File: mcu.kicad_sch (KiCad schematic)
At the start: 25 parts, among them J1 Conn_01x05, J4 USB_B_Micro, U1 STM32G473CCUx, Y1 8 MHz

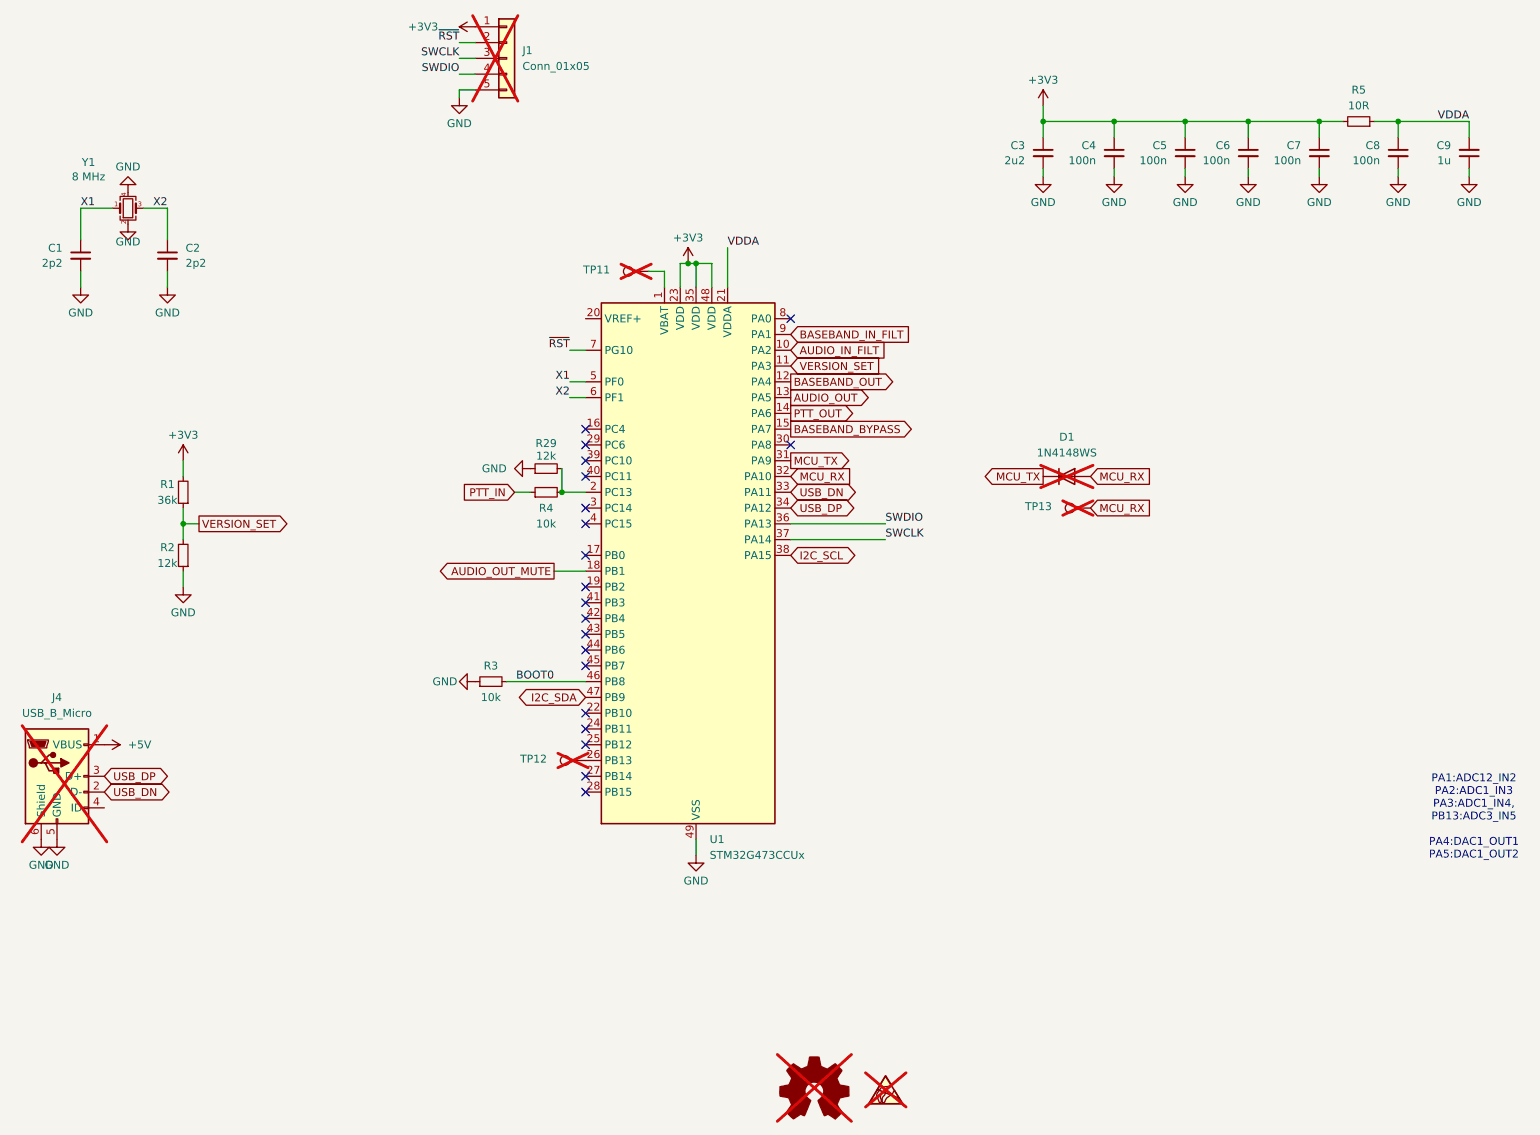
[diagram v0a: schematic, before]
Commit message: cosmetic changes to the schematic layout
- R25 - DNP
- PDF render update
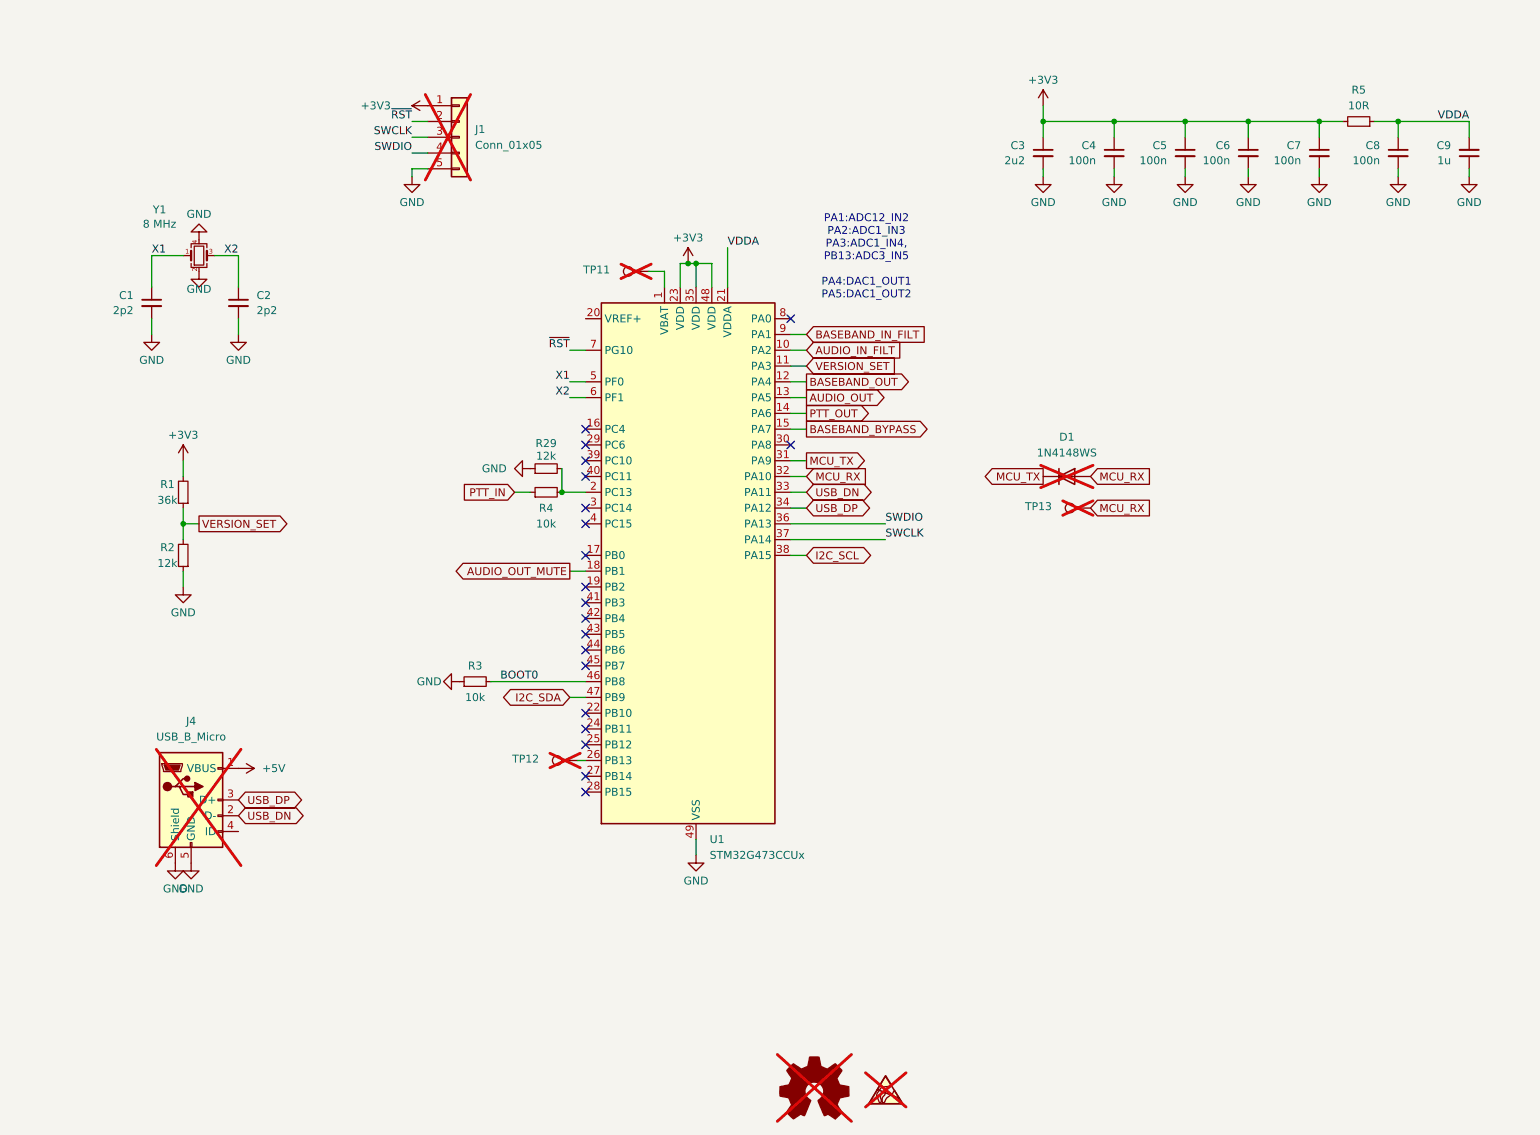
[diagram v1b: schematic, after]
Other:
- company: Wojciech Kaczmarski SP5WWP et al. -> Wojciech SP5WWP, Mano ON6RF, Mutlu TA1MD et al.
- title: Micro17 - OpenRTX on a Module for Icom Radios -> Micro17 - OpenRTX on a Module for ICOM radios
- moved on the sheet: C1, C2, J1, J4, R3, TP12, Y1

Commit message: Bias voltage changed, usart rx tp add
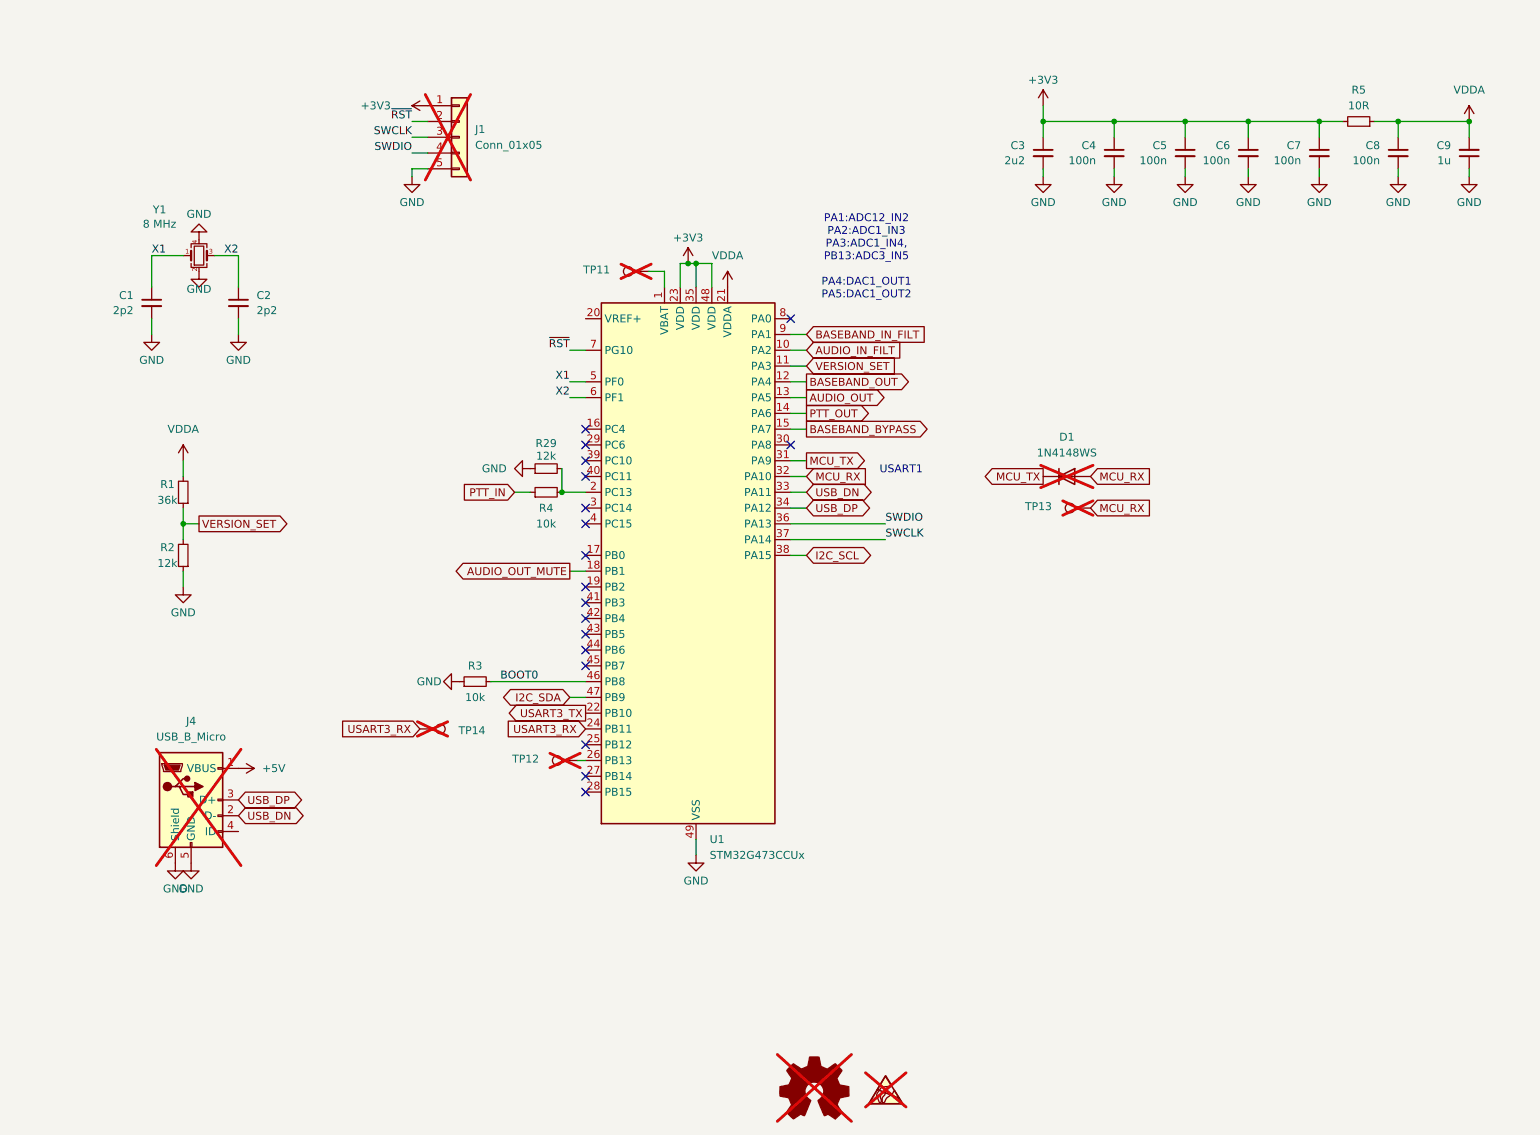
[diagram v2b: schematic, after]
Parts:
- added TP14: GP, TestPoint:TestPoint_Pad_D1.0mm, symbol Connector:TestPoint
- C1, C2: MPN (none) -> C1559
- C3: MPN (none) -> C170151
- C4, C5, C6, C7, C8: MPN (none) -> C56392
- C9: MPN (none) -> C29266
- D1, J1: now left out of the parts list
- R1: MPN (none) -> C4354982
- R2, R29: MPN (none) -> C25752
- R3, R4: MPN (none) -> C102749
- R5: MPN (none) -> C854481
- U1: MPN (none) -> C1342773
- Y1: MPN TX32258M4DBDD2T -> C5308002
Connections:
- net +3V3: no longer R1.2
- net VDDA: now also R1.2
- net USART3_TX: now reaches U1.22 (PB10)
- net USART3_RX: now reaches U1.24 (PB11)
- net USART3_RX: now also TP14.1
- no-connect marks 20 -> 18
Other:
- note added: "USART1"

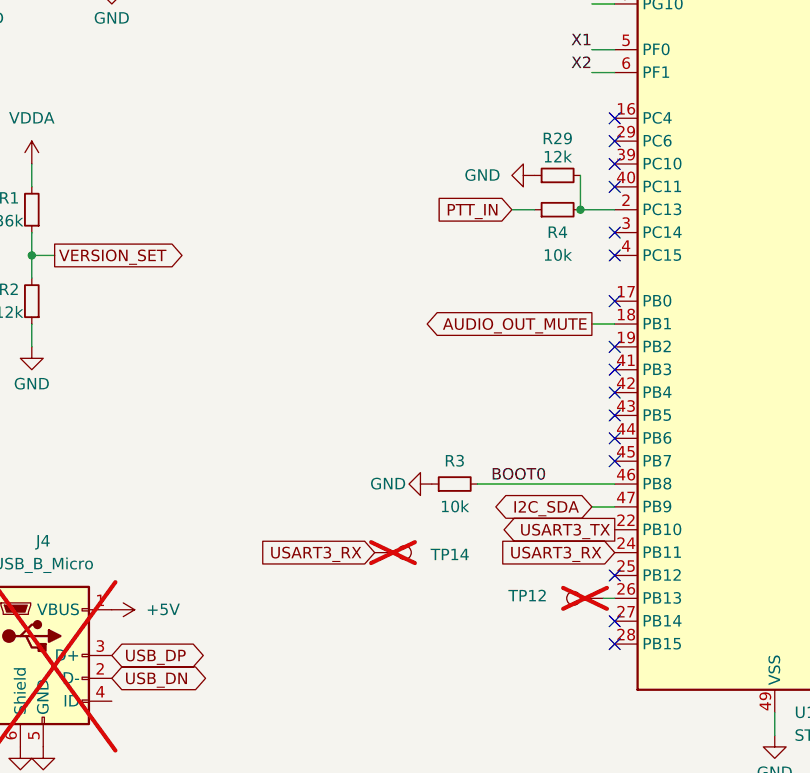
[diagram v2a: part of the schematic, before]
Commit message: R30 Added
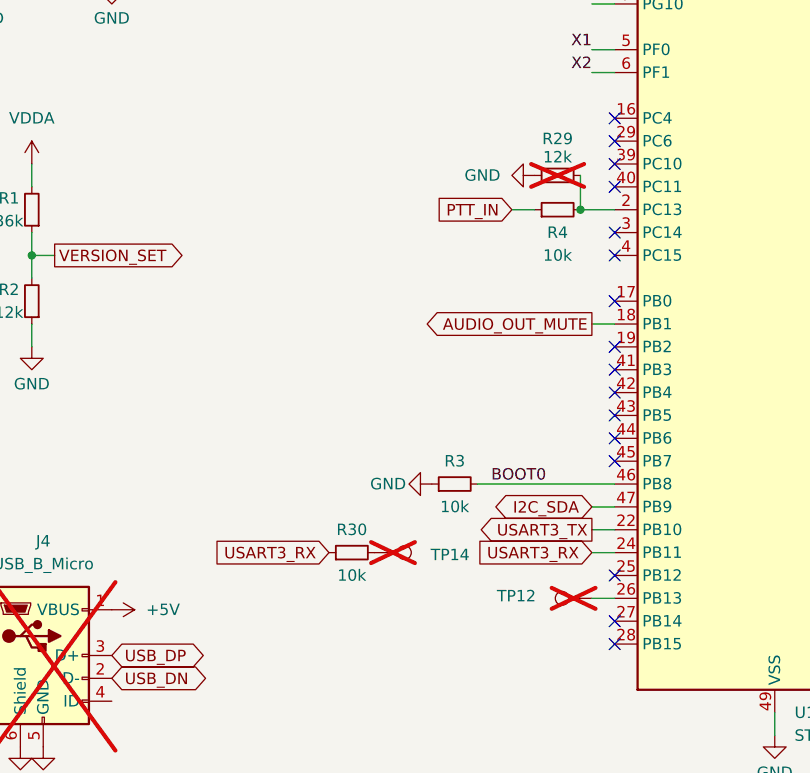
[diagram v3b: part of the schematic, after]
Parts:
- added R30: 10k, Resistor_SMD:R_0402_1005Metric, symbol Device:R_Small
- R29: now not fitted; now left out of the parts list
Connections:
- net USART3_RX: now also R30.1; no longer TP14.1
- new net: R30.2, TP14.1
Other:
- moved on the sheet: TP12
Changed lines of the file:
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@@
 	(wire
 		(pts
+			(xy 119.38 132.08) (xy 121.92 132.08)
+		)
+		(stroke
+			(width 0)
+			(type default)
+		)
+	)
+	(wire
+		(pts
 			(xy 207.01 34.29) (xy 195.58 34.29)
 		)
@@
 	(wire
 		(pts
+			(xy 119.38 129.54) (xy 121.92 129.54)
+		)
+		(stroke
+			(width 0)
+			(type default)
+		)
+	)
+	(wire
+		(pts
 			(xy 195.58 34.29) (xy 195.58 31.75)
 		)
@@
 	(wire
 		(pts
-			(xy 120.65 137.16) (xy 121.92 137.16)
+			(xy 119.38 137.16) (xy 121.92 137.16)
 		)
 		(stroke
@@
 	(global_label "USART3_RX"
 		(shape input)
-		(at 121.92 132.08 180)
+		(at 119.38 132.08 180)
 		(fields_autoplaced yes)
 		(effects
@@
 		)
 		(property "Intersheetrefs" "${INTERSHEET_REFS}"
-			(at 108.412 132.08 0)
+			(at 105.872 132.08 0)
 			(effects
 				(font
@@
 	(global_label "USART3_RX"
 		(shape input)
-		(at 95.25 132.08 180)
+		(at 90.17 132.08 180)
 		(fields_autoplaced yes)
 		(effects
@@
 		)
 		(property "Intersheetrefs" "${INTERSHEET_REFS}"
-			(at 81.742 132.08 0)
+			(at 76.662 132.08 0)
 			(effects
 				(font
@@
 	(global_label "USART3_TX"
 		(shape output)
-		(at 121.92 129.54 180)
+		(at 119.38 129.54 180)
 		(fields_autoplaced yes)
 		(effects
@@
 		)
 		(property "Intersheetrefs" "${INTERSHEET_REFS}"
-			(at 108.7144 129.54 0)
+			(at 106.1744 129.54 0)
 			(effects
 				(font
@@
 	(symbol
 		(lib_id "Connector:TestPoint")
-		(at 120.65 137.16 90)
+		(at 119.38 137.16 90)
 		(unit 1)
 		(exclude_from_sim no)
@@
 		(dnp yes)
 		(property "Reference" "TP12"
-			(at 112.268 136.906 90)
+			(at 110.998 136.906 90)
 			(effects
 				(font
@@
 		)
 		(property "Value" "GP"
-			(at 115.57 135.8901 90)
+			(at 114.3 135.8901 90)
 			(effects
 				(font
@@
 		)
 		(property "Footprint" "TestPoint:TestPoint_Pad_D1.0mm"
-			(at 120.65 132.08 0)
+			(at 119.38 132.08 0)
 			(effects
 				(font
@@
 		)
 		(property "Datasheet" "~"
-			(at 120.65 132.08 0)
+			(at 119.38 132.08 0)
 			(effects
 				(font
@@
 		)
 		(property "Description" ""
-			(at 120.65 137.16 0)
+			(at 119.38 137.16 0)
 			(effects
 				(font
@@
 		)
 		(property "MPN" ""
-			(at 120.65 137.16 0)
+			(at 119.38 137.16 0)
 			(effects
 				(font
@@
 		)
 		(property "Height" ""
-			(at 120.65 137.16 0)
+			(at 119.38 137.16 0)
 			(effects
 				(font
@@
 		)
 		(property "Manufacturer_Name" ""
-			(at 120.65 137.16 0)
+			(at 119.38 137.16 0)
 			(effects
 				(font
@@
 		)
 		(property "Manufacturer_Part_Number" ""
-			(at 120.65 137.16 0)
+			(at 119.38 137.16 0)
 			(effects
 				(font
@@
 		)
 		(property "Mouser Part Number" ""
-			(at 120.65 137.16 0)
+			(at 119.38 137.16 0)
 			(effects
 				(font
@@
 		)
 		(property "Mouser Price/Stock" ""
-			(at 120.65 137.16 0)
+			(at 119.38 137.16 0)
 			(effects
 				(font
@@
 		)
 		(property "JLC" ""
-			(at 120.65 137.16 0)
+			(at 119.38 137.16 0)
 			(effects
 				(font
@@
 		)
 		(property "PN" ""
-			(at 120.65 137.16 0)
+			(at 119.38 137.16 0)
 			(effects
 				(font
@@
 		(unit 1)
 		(exclude_from_sim no)
-		(in_bom yes)
+		(in_bom no)
 		(on_board yes)
-		(dnp no)
+		(dnp yes)
 		(property "Reference" "R29"
 			(at 115.57 86.106 90)
@@
 					(unit 1)
 				)
+			)
+		)
+	)
+	(symbol
+		(lib_id "Device:R_Small")
+		(at 92.71 132.08 90)
+		(unit 1)
+		(exclude_from_sim no)
+		(in_bom yes)
+		(on_board yes)
+		(dnp no)
+		(property "Reference" "R30"
+			(at 92.71 129.54 90)
+			(effects
+				(font
+					(size 1.27 1.27)
+				)
+			)
+		)
+		(property "Value" "10k"
+			(at 92.71 134.62 90)
+			(effects
+				(font
+					(size 1.27 1.27)
+				)
+			)
+		)
+		(property "Footprint" "Resistor_SMD:R_0402_1005Metric"
+			(at 92.71 132.08 0)
+			(effects
+				(font
+					(size 1.27 1.27)
+				)
+				(hide yes)
+			)
+		)
+		(property "Datasheet" "~"
+			(at 92.71 132.08 0)
+			(effects
+				(font
+					(size 1.27 1.27)
+				)
+				(hide yes)
+			)
+		)
+		(property "Description" ""
+			(at 92.71 132.08 0)
+			(effects
+				(font
+					(size 1.27 1.27)
+				)
+				(hide yes)
+			)
+		)
+		(property "MPN" "C102749"
+			(at 92.71 132.08 90)
+			(effects
+				(font
+					(size 1.27 1.27)
+				)
+				(hide yes)
+			)
+		)
+		(property "Height" ""
+			(at 92.71 132.08 0)
+			(effects
+				(font
+					(size 1.27 1.27)
+				)
+				(hide yes)
+			)
+		)
+		(property "Manufacturer_Name" ""
+			(at 92.71 132.08 0)
+			(effects
+				(font
+					(size 1.27 1.27)
+				)
+				(hide yes)
+			)
+		)
+		(property "Manufacturer_Part_Number" ""
+			(at 92.71 132.08 0)
+			(effects
+				(font
+					(size 1.27 1.27)
+				)
+				(hide yes)
+			)
+		)
+		(property "Mouser Part Number" ""
+			(at 92.71 132.08 0)
+			(effects
+				(font
+					(size 1.27 1.27)
+				)
+				(hide yes)
+			)
+		)
+		(property "Mouser Price/Stock" ""
+			(at 92.71 132.08 0)
+			(effects
+				(font
+					(size 1.27 1.27)
+				)
+				(hide yes)
+			)
+		)
+		(property "LCSC" "C102749"
+			(at 92.71 132.08 0)
+			(effects
+				(font
+					(size 1.27 1.27)
+				)
+				(hide yes)
+			)
+		)
+		(property "JLC" ""
+			(at 92.71 132.08 0)
+			(effects
+				(font
+					(size 1.27 1.27)
+				)
+				(hide yes)
+			)
+		)
+		(property "PN" ""
+			(at 92.71 132.08 0)
+			(effects
+				(font
+					(size 1.27 1.27)
+				)
+				(hide yes)
+			)
+		)
+		(pin "1"
+		)
+		(pin "2"
+		)
+		(instances
+			(project "micro17"
+				(path "/8b0d7f56-1962-40c9-8b95-6d4fe558acbc/9f9e0b5b-f07d-4ebd-b315-be375c62719d"
+					(reference "R30")
+					(unit 1)
+				)
